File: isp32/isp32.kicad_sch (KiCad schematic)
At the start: 89 parts, among them J1 BAT1, J2 Switching, J3 USB_C_Receptacle_USB2.0, J4 ESP_JTAG, J5 GPS_ANT, J6 F0, J7 F1, J8 Flash_SPI, J9 Conn_01x12, Q1 BSS138, Q2 BSS138, Q3 IRLML6402, Q4 BSS138, Q5 IRLML6402, Q6 S8050, Q7 S8050, Q8 S8050, SW1 RST, SW2 IO0, U10 BMP280, U11 MPU-9250, U12 CH340C, U2 USBLC6-2SC6, U3 ESP32-WROOM-32U, U4 AMS1117-3.3, U5 MP2303ADN, U7 NEO-XM, U8 AT25SF081-SSHD-X, U9 RFM98W-315S2

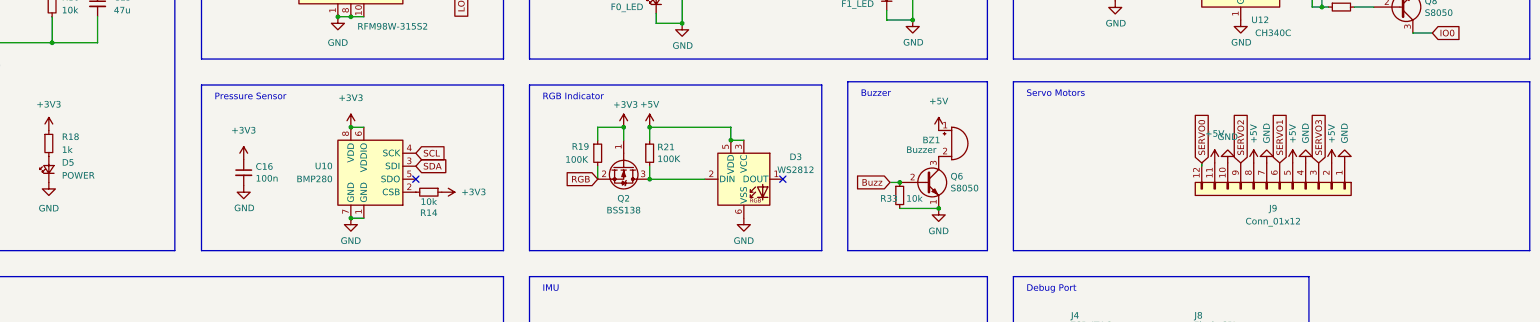
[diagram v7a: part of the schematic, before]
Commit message: Split motor and add tp
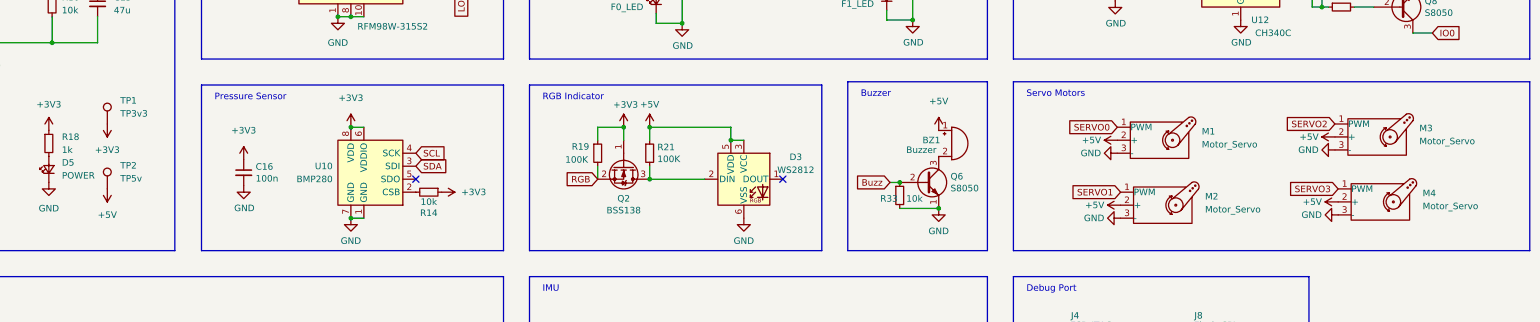
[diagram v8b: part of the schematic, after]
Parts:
- removed J9: Conn_01x12, Connector_PinHeader_2.54mm:PinHeader_1x12_P2.54mm_Horizontal, symbol Connector_Generic:Conn_01x12
- added M1, M2, M3, M4: Motor_Servo, Connector_PinHeader_2.54mm:PinHeader_1x03_P2.54mm_Vertical, symbol Motor:Motor_Servo
- added TP1: TP3v3, TestPoint:TestPoint_Pad_D1.0mm, symbol Connector:TestPoint
- added TP2: TP5v, TestPoint:TestPoint_Pad_D1.0mm, symbol Connector:TestPoint
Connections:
- net +3V3: now also TP1.1
- net +5V: now also M1.2 (+), M2.2 (+), M3.2 (+), M4.2 (+), TP2.1
- net GND: now also M1.3 (-), M2.3 (-), M3.3 (-), M4.3 (-)
- net SERVO0: now also M1.1 (PWM)
- net SERVO1: now also M2.1 (PWM)
- net SERVO2: now also M3.1 (PWM)
- net SERVO3: now also M4.1 (PWM)
